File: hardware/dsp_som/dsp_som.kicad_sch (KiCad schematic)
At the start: 0 parts

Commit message: Tests
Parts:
- added C1: 2u2, Capacitor_SMD:C_0603_1608Metric, symbol Device:C_Small
- added FB1: 600R, Inductor_SMD:L_0603_1608Metric, symbol Device:FerriteBead_Small
- added H1: MountingHole_Pad, MountingHole:MountingHole_3.2mm_M3_Pad_Via, symbol Mechanical:MountingHole_Pad
- added J1: Micro_SD_Card_Det_Hirose_DM3AT, Connector_Card:microSD_HC_Hirose_DM3AT-SF-PEJM5, symbol Connector:Micro_SD_Card_Det_Hirose_DM3AT
- added J2: Conn_02x07_Odd_Even, Connector_PinHeader_1.27mm:PinHeader_2x07_P1.27mm_Vertical_SMD, symbol Connector_Generic:Conn_02x07_Odd_Even
- added J3: Conn_02x22_Odd_Even, Connector_PinHeader_2.54mm:PinHeader_2x22_P2.54mm_Vertical, symbol Connector_Generic:Conn_02x22_Odd_Even
- added U1: IS42S16400J-xT, Package_SO:TSOP-II-54_22.2x10.16mm_P0.8mm, symbol Memory_RAM:IS42S16400J-xT
- added U2: SGTL5000XNAA3, Package_DFN_QFN:QFN-32-1EP_5x5mm_P0.5mm_EP3.6x3.6mm, symbol Audio:SGTL5000XNAA3
- added U4: BU18SD2MG-MTR, Package_TO_SOT_SMD:SOT-23-5, symbol WITNS_ROHM:BU18SD2MG-MTR
- added U5: STM32F446ZCTx, Package_QFP:LQFP-144_20x20mm_P0.5mm, symbol MCU_ST_STM32F4:STM32F446ZCTx
- added Y1: 16MHz, Crystal:Crystal_SMD_EuroQuartz_MT-4Pin_3.2x2.5mm, symbol Device:Crystal_GND24_Small
- added Y3: 32kHz768, Crystal:Crystal_SMD_3215-2Pin_3.2x1.5mm, symbol Device:Crystal_Small
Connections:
- new net: U1.1 (VDD), U1.14 (VDD), U1.27 (VDD)
- new net: U1.12 (GNDQ), U1.46 (GNDQ), U1.52 (GNDQ), U1.6 (GNDQ)
- new net: U1.28 (GND), U1.41 (GND), U1.54 (GND)
- new net: U1.3 (VDDQ), U1.43 (VDDQ), U1.49 (VDDQ), U1.9 (VDDQ)
- new net: U5.107 (VSS), U5.120 (VSS), U5.130 (VSS), U5.16 (VSS), U5.38 (VSS), U5.51 (VSS), U5.61 (VSS), U5.83 (VSS), U5.94 (VSS)
- new net: U2.1 (GND), U2.3 (GND), U2.33 (GND)
- new net +3.3V: FB1.1
- new net +3.3VA: C1.1, FB1.2
- new net GND: C1.2, H1.1
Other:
- note added: "Farnell : 2101347"

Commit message: 1st attempt at routing the SDRAM
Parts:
- added C10, C11, C12, C13, C14, C15, C2, C22, C23, C24, C25, C26, C27, C28, C29, C3, C31, C4, C5, C6, C7, C8, C9: 100n, Capacitor_SMD:C_0402_1005Metric, symbol Device:C_Small
- added C16, C30, C32, C33, C34: 1u, Capacitor_SMD:C_0603_1608Metric, symbol Device:C_Small
- added C17: 4.7u, Capacitor_SMD:C_0603_1608Metric, symbol Device:C_Small
- added C18, C19: 10p, Capacitor_SMD:C_0402_1005Metric, symbol Device:C_Small
- added C20, C21: ??, Capacitor_SMD:C_0402_1005Metric, symbol Device:C_Small
- added R1: 10R, Resistor_SMD:R_0402_1005Metric, symbol Device:R_Small
- added R2: 100k, Resistor_SMD:R_0402_1005Metric, symbol Device:R_Small
- J2: value Conn_02x07_Odd_Even -> SWD
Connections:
- net +3.3V: now also J2.3 (Pin_3), U1.1 (VDD), U1.14 (VDD), U1.27 (VDD), U1.3 (VDDQ), U1.43 (VDDQ), U1.49 (VDDQ), U1.9 (VDDQ), U4.1 (IN), U4.3 (STBY), U5.108 (VDD), U5.121 (VDD), U5.131 (VDD), U5.143 (PDR_ON), U5.144 (VDD), U5.17 (VDD), U5.30 (VDD), U5.32 (VREF+), U5.39 (VDD), U5.52 (VDD), U5.6 (VBAT), U5.62 (VDD), U5.72 (VDD), U5.84 (VDD), U5.95 (VDDUSB), C10.1, C11.1, C12.1, C13.1, C14.1, C17.1, C22.1, C23.1, C24.1, C25.1, C26.1, C27.1, C28.1, C29.1, C3.1, C30.1, C31.1, C32.1, C33.1, C4.1, C5.1, C6.1, C7.1, C8.1, C9.1
- net +3.3VA: now also U5.33 (VDDA), C15.1, C16.1
- net GND: now also J2.11 (Pin_11), J2.5 (Pin_5), J2.7 (Pin_7), U1.12 (GNDQ), U1.28 (GND), U1.41 (GND), U1.46 (GNDQ), U1.52 (GNDQ), U1.54 (GND), U1.6 (GNDQ), U2.1 (GND), U2.3 (GND), U2.33 (GND), U2.7 (AGND), U4.2 (GND), U5.107 (VSS), U5.120 (VSS), U5.130 (VSS), U5.16 (VSS), U5.31 (VSSA), U5.38 (VSS), U5.51 (VSS), U5.61 (VSS), U5.83 (VSS), U5.94 (VSS), Y1.2, Y1.4, C10.2, C11.2, C12.2, C13.2, C14.2, C15.2, C16.2, C17.2, C18.1, C19.1, C2.2, C20.2, C21.2, C22.2, C23.2, C24.2, C25.2, C26.2, C27.2, C28.2, C29.2, C3.2, C30.2, C31.2, C32.2, C33.2, C34.2, C4.2, C5.2, C6.2, C7.2, C8.2, C9.2, R2.1
- net DQ5: now reaches U1.10 (DQ5)
- net DQ5: now also U5.59 (PE8)
- net DQ6: now reaches U1.11 (DQ6)
- net DQ6: now also U5.60 (PE9)
- net DQ7: now reaches U1.13 (DQ7)
- net DQ7: now also U5.63 (PE10)
- net LDQM: now reaches U1.15 (LDQM)
- net LDQM: now also U5.141 (PE0)
- net nWE: now reaches U1.16 (~{WE})
- net nWE: now also U5.26 (PC0)
- net nCAS: now reaches U1.17 (~{CAS})
- net nCAS: now also U5.132 (PG15)
- net nRAS: now reaches U1.18 (~{RAS})
- net nRAS: now also U5.49 (PF11)
- net nCS: now reaches U1.19 (~{CS})
- net nCS: now also U5.136 (PB6)
- net DQ0: now reaches U1.2 (DQ0)
- net DQ0: now also U5.85 (PD14)
- net BA0: now reaches U1.20 (BA0)
- net BA0: now also U5.89 (PG4)
- net BA1: now reaches U1.21 (BA1)
- net BA1: now also U5.90 (PG5)
- net A10: now reaches U1.22 (A10)
- net A10: now also U5.56 (PG0)
- net A0: now reaches U1.23 (A0)
- net A0: now also U5.10 (PF0)
- net A1: now reaches U1.24 (A1)
- net A1: now also U5.11 (PF1)
- net A2: now reaches U1.25 (A2)
- net A2: now also U5.12 (PF2)
- net A3: now reaches U1.26 (A3)
- net A3: now also U5.13 (PF3)
- net A4: now reaches U1.29 (A4)
- net A4: now also U5.14 (PF4)
- net A5: now reaches U1.30 (A5)
- net A5: now also U5.15 (PF5)
- net A6: now reaches U1.31 (A6)
- net A6: now also U5.50 (PF12)
- net A7: now reaches U1.32 (A7)
- net A7: now also U5.53 (PF13)
- net A8: now reaches U1.33 (A8)
- net A8: now also U5.54 (PF14)
- net A9: now reaches U1.34 (A9)
- net A9: now also U5.55 (PF15)
- net A11: now reaches U1.35 (A11)
- net A11: now also U5.57 (PG1)
- net CKE: now reaches U1.37 (CKE)
- net CKE: now also U5.135 (PB5)
- net CLK: now reaches U1.38 (CLK)
- net CLK: now also U5.93 (PG8)
- net UDQM: now reaches U1.39 (UDQM)
- net UDQM: now also U5.142 (PE1)
- net DQ1: now reaches U1.4 (DQ1)
- net DQ1: now also U5.86 (PD15)
- net DQ8: now reaches U1.42 (DQ8)
- net DQ8: now also U5.64 (PE11)
- net DQ9: now reaches U1.44 (DQ9)
- net DQ9: now also U5.65 (PE12)
- net DQ10: now reaches U1.45 (DQ10)
- net DQ10: now also U5.66 (PE13)
- net DQ11: now reaches U1.47 (DQ11)
- net DQ11: now also U5.67 (PE14)
- net DQ12: now reaches U1.48 (DQ12)
- net DQ12: now also U5.68 (PE15)
- net DQ2: now reaches U1.5 (DQ2)
- net DQ2: now also U5.114 (PD0)
- net DQ13: now reaches U1.50 (DQ13)
- net DQ13: now also U5.77 (PD8)
- net DQ14: now reaches U1.51 (DQ14)
- net DQ14: now also U5.78 (PD9)
- net DQ15: now reaches U1.53 (DQ15)
- net DQ15: now also U5.79 (PD10)
- net DQ3: now reaches U1.7 (DQ3)
- net DQ3: now also U5.115 (PD1)
- net DQ4: now reaches U1.8 (DQ4)
- net DQ4: now also U5.58 (PE7)
- net nRST: now reaches J2.12 (Pin_12)
- net nRST: now also U5.25 (NRST), C2.1
- net VCP_RX: now reaches J2.13 (Pin_13)
- net VCP_TX: now reaches J2.14 (Pin_14)
- net SWDIO: now reaches J2.4 (Pin_4)
- net SWDIO: now also U5.105 (PA13)
- net SWCLK: now reaches J2.6 (Pin_6)
- net SWCLK: now also U5.109 (PA14)
- net SWO: now reaches J2.8 (Pin_8)
- net SWO: now also U5.133 (PB3)
- net XTAL_OUT: now reaches Y1.1
- net XTAL_OUT: now also C19.2, R1.1
- net OSC_IN: now reaches Y1.3
- net OSC_IN: now also U5.23 (PH0), C18.2
- net BOOT0: now reaches U5.138 (BOOT0)
- net BOOT0: now also R2.2
- net OSC_OUT: now reaches U5.24 (PH1)
- net OSC_OUT: now also R1.2
- net OSC32_IN: now reaches U5.8 (PC14)
- net OSC32_IN: now also Y3.2, C20.1
- net OSC32_OUT: now reaches U5.9 (PC15)
- net OSC32_OUT: now also Y3.1, C21.1
- net +1V8: now reaches U4.5 (OUT)
- net +1V8: now also C34.1
- no-connect marks 0 -> 4
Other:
- note added: "Boot from Flash"
- note added: "Can't move"
- note added: "NBL0"
- note added: "NBL1"
- note added: "PA7/PC0"
- note added: "SDCKE1"
- note added: "SDCLK"
- note added: "SDNCAS"
- note added: "SDNE1"
- note added: "SDNRAS"
- note added: "SDNWE"
- moved on the sheet: J2, U1, U5, Y1, Y3

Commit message: routing 1st version
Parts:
- added C35, C36, C37, C38: 100n, Capacitor_SMD:C_0402_1005Metric, symbol Device:C_Small
- added C39, C40: 2.2u, Capacitor_SMD:C_0603_1608Metric, symbol Device:C_Small
- added R3, R4, R5, R6, R7: 47k, Resistor_SMD:R_0402_1005Metric, symbol Device:R_Small
- added R8, R9: 1.5k, Resistor_SMD:R_0402_1005Metric, symbol Device:R_Small
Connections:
- net +1V8: now also U2.30 (VDDD), C38.1
- net +3.3V: now also J1.4 (VDD), J3.1 (Pin_1), U2.20 (VDDIO), C35.1, R3.1, R4.1, R5.1, R6.1, R7.1, R8.1, R9.1
- net +3.3VA: now also U2.5 (VDDA), C37.1
- net GND: now also J1.11 (SHIELD), J1.6 (VSS), J1.9 (DET_B), J3.10 (Pin_10), J3.12 (Pin_12), J3.14 (Pin_14), J3.16 (Pin_16), J3.18 (Pin_18), J3.2 (Pin_2), J3.20 (Pin_20), J3.22 (Pin_22), J3.24 (Pin_24), J3.26 (Pin_26), J3.28 (Pin_28), J3.30 (Pin_30), J3.32 (Pin_32), J3.34 (Pin_34), J3.35 (Pin_35), J3.36 (Pin_36), J3.38 (Pin_38), J3.4 (Pin_4), J3.40 (Pin_40), J3.42 (Pin_42), J3.44 (Pin_44), J3.6 (Pin_6), J3.8 (Pin_8), U2.31 (CTRL_ADR0_CS), U2.32 (CTRL_MODE), C35.2, C36.2, C37.2, C38.2, C39.2, C40.2
- net VCP_RX: now also U5.35 (PA1)
- net VCP_TX: now also U5.34 (PA0)
- net SD_DAT2: now reaches J1.1 (DAT2)
- net SD_DAT2: now also U5.111 (PC10), R7.2
- net SD_DETECT: now reaches J1.10 (DET_A)
- net SD_DETECT: now also U5.137 (PB7)
- net SD_DAT3: now reaches J1.2 (DAT3/CD)
- net SD_DAT3: now also U5.112 (PC11), R6.2
- net SD_CMD: now reaches J1.3 (CMD)
- net SD_CMD: now also U5.116 (PD2), R5.2
- net SD_CLK: now reaches J1.5 (CLK)
- net SD_CLK: now also U5.113 (PC12)
- net SD_DAT0: now reaches J1.7 (DAT0)
- net SD_DAT0: now also U5.98 (PC8), R4.2
- net SD_DAT1: now reaches J1.8 (DAT1)
- net SD_DAT1: now also U5.99 (PC9), R3.2
- net CODEC_MCLK: now reaches U5.1 (PE2)
- net CODEC_MCLK: now also U2.21 (SYS_MCLK)
- net USB_DM: now reaches U5.103 (PA11)
- net USB_DM: now also J3.25 (Pin_25)
- net USB_DP: now reaches U5.104 (PA12)
- net USB_DP: now also J3.27 (Pin_27)
- net VCAP_2: now reaches U5.106 (VCAP_2)
- net VCAP_2: now also C39.1
- net CODEC_SCL: now reaches U5.139 (PB8)
- net CODEC_SCL: now also U2.29 (CTRL_CLK), R8.2
- net CODEC_SDA: now reaches U5.140 (PB9)
- net CODEC_SDA: now also U2.27 (CTRL_DATA), R9.2
- net ADC3_IN4: now reaches U5.18 (PF6)
- net ADC3_IN4: now also J3.33 (Pin_33)
- net ADC3_IN5: now reaches U5.19 (PF7)
- net ADC3_IN5: now also J3.31 (Pin_31)
- net CODEC_DOUT: now reaches U5.2 (PE3)
- net CODEC_DOUT: now also U2.25 (I2S_DOUT)
- net ADC3_IN6: now reaches U5.20 (PF8)
- net ADC3_IN6: now also J3.29 (Pin_29)
- net ADC3_IN7: now reaches U5.21 (PF9)
- net ADC3_IN7: now also J3.23 (Pin_23)
- net ADC3_IN8: now reaches U5.22 (PF10)
- net ADC3_IN8: now also J3.21 (Pin_21)
- net ADC3_IN11: now reaches U5.27 (PC1)
- net ADC3_IN11: now also J3.19 (Pin_19)
- net ADC3_IN12: now reaches U5.28 (PC2)
- net ADC3_IN12: now also J3.17 (Pin_17)
- net ADC3_IN13: now reaches U5.29 (PC3)
- net ADC3_IN13: now also J3.15 (Pin_15)
- net CODEC_LRCLK: now reaches U5.3 (PE4)
- net CODEC_LRCLK: now also U2.23 (I2S_LRCLK)
- net ADC3_IN2: now reaches U5.36 (PA2)
- net ADC3_IN2: now also J3.11 (Pin_11)
- net ADC3_IN3: now reaches U5.37 (PA3)
- net ADC3_IN3: now also J3.13 (Pin_13)
- net CODEC_SCLK: now reaches U5.4 (PE5)
- net CODEC_SCLK: now also U2.24 (I2S_SCLK)
- net CODEC_DIN: now reaches U5.5 (PE6)
- net CODEC_DIN: now also U2.26 (I2S_DIN)
- net PB10: now reaches U5.69 (PB10)
- net PB10: now also J3.3 (Pin_3)
- net PB11: now reaches U5.70 (PB11)
- net PB11: now also J3.5 (Pin_5)
- net VCAP_1: now reaches U5.71 (VCAP_1)
- net VCAP_1: now also C40.1
- net PD12: now reaches U5.81 (PD12)
- net PD12: now also J3.7 (Pin_7)
- net PD13: now reaches U5.82 (PD13)
- net PD13: now also J3.9 (Pin_9)
- net LINEOUT_R: now reaches J3.37 (Pin_37)
- net LINEOUT_R: now also U2.11 (LINEOUT_R)
- net LINEOUT_L: now reaches J3.39 (Pin_39)
- net LINEOUT_L: now also U2.12 (LINEOUT_L)
- net LINEIN_R: now reaches J3.41 (Pin_41)
- net LINEIN_R: now also U2.13 (LINEIN_R)
- net LINEIN_L: now reaches J3.43 (Pin_43)
- net LINEIN_L: now also U2.14 (LINEIN_L)
- net VAG: now reaches U2.10 (VAG)
- net VAG: now also C36.1
- no-connect marks 4 -> 47
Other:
- note added: "I2C Mode"
- note added: "VDDIO & VDDA to 3.3V => No CPFILT"
- note removed: "Can't move"
- moved on the sheet: C1, C33, C34, FB1, J3, U2, U4

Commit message: gnd vias
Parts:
- J3: value Conn_02x22_Odd_Even -> DSP_SoM Connector
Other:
- note added: "CODEC VDDD LDO"
- note added: "DSP SoM Connector"
- note added: "Micro SD-Card Socket"
- note added: "Mounting Hole"
- note added: "SDRAM"
- note added: "SGTL5000 Audio CODEC"
- note added: "SWD Connector for STLINK"
- note added: "The STM32"
- note added: "VDDA Filtering"
- company: (none) -> WITNS
- title: (none) -> DSP SoM
- moved on the sheet: C1, C10, C11, C12, C13, C14, C15, C16, C17, C18, C19, C2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

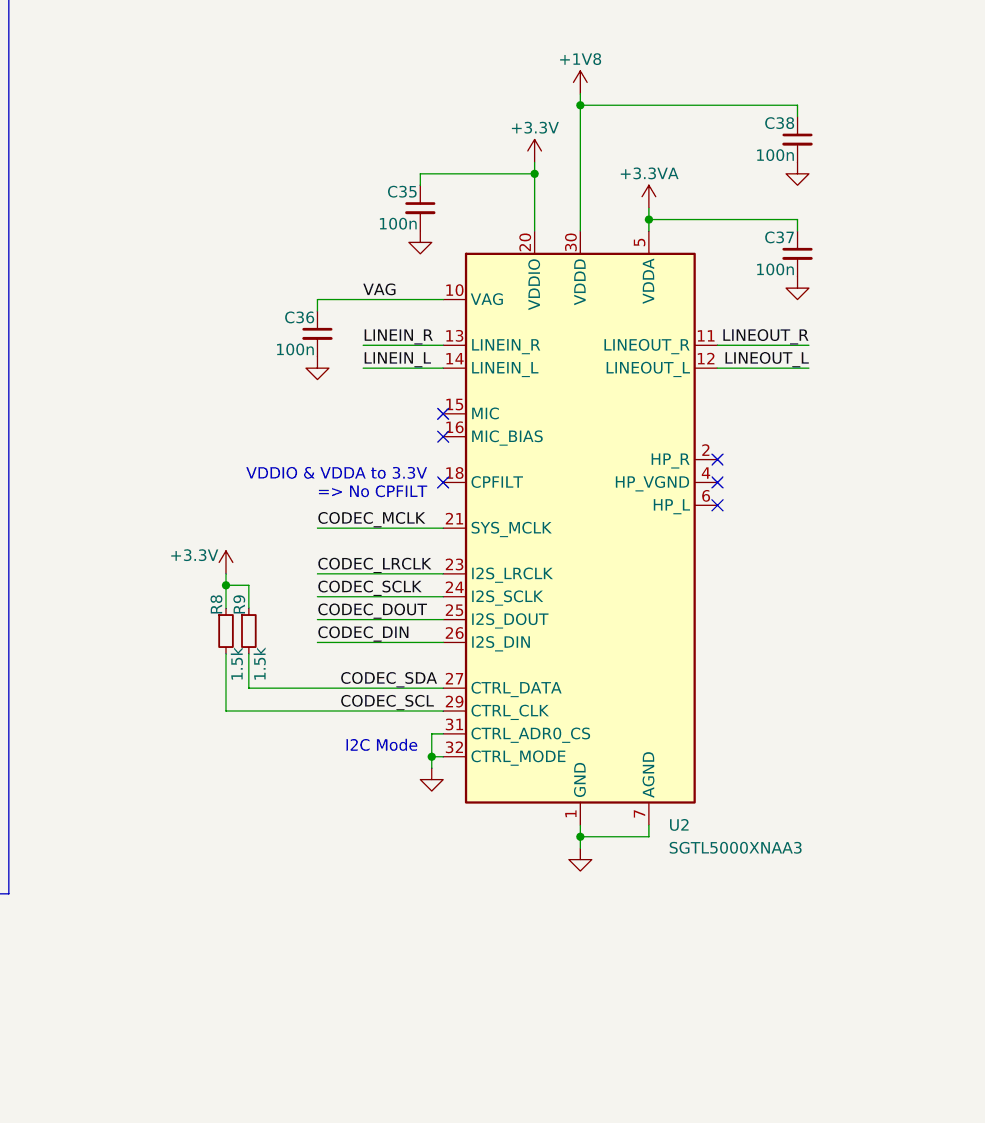
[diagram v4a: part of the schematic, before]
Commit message: Change SGTL5000 model due to obsolescence
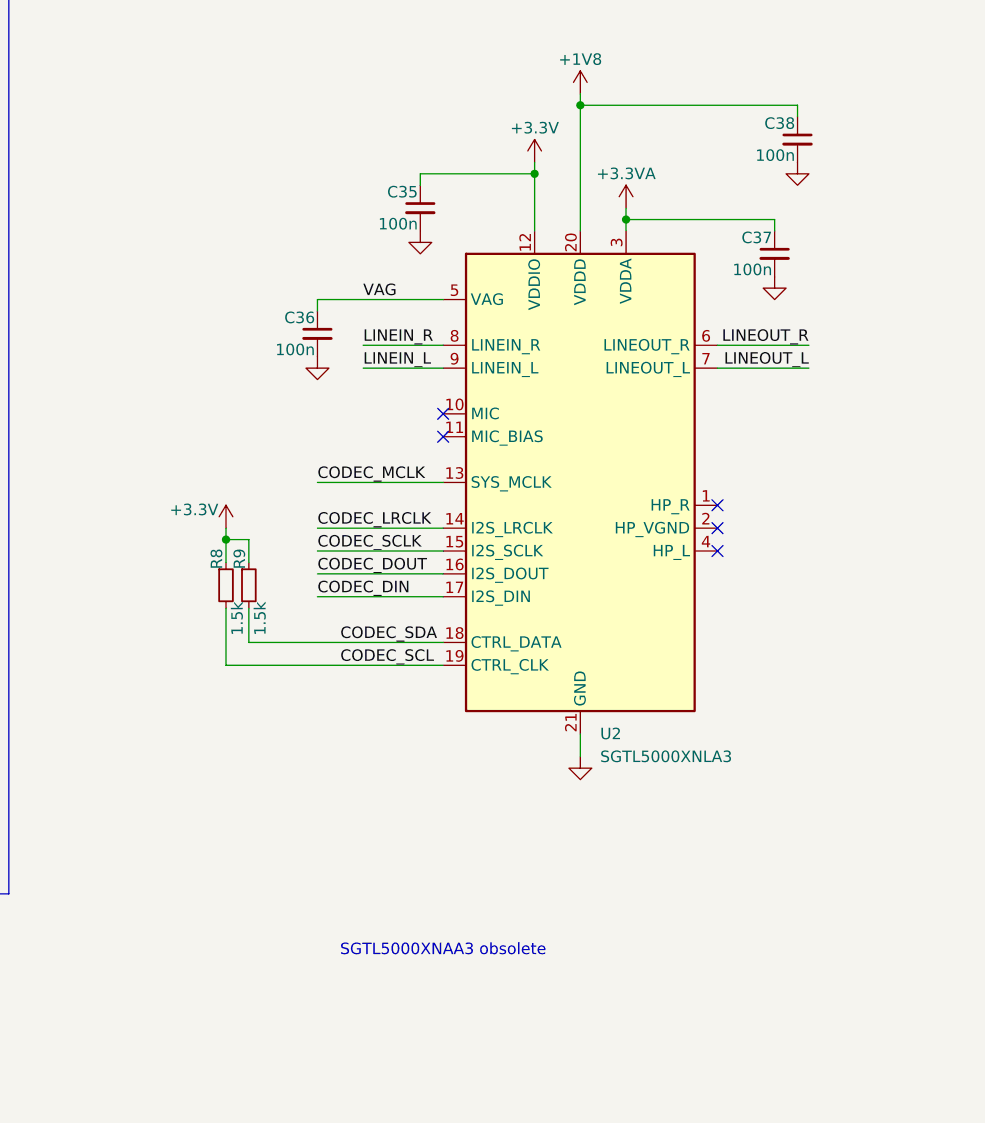
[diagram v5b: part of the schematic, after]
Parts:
- removed U2: SGTL5000XNAA3, Package_DFN_QFN:QFN-32-1EP_5x5mm_P0.5mm_EP3.6x3.6mm, symbol Audio:SGTL5000XNAA3
- added U2: SGTL5000XNLA3, Package_DFN_QFN:QFN-20-1EP_3x3mm_P0.4mm_EP1.65x1.65mm, symbol Audio:SGTL5000XNLA3
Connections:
- net +1V8: now also U2.20 (VDDD)
- net +3.3V: now also U2.12 (VDDIO)
- net +3.3VA: now also U2.3 (VDDA)
- net CODEC_DIN: now also U2.17 (I2S_DIN)
- net CODEC_DOUT: now also U2.16 (I2S_DOUT)
- net CODEC_LRCLK: now also U2.14 (I2S_LRCLK)
- net CODEC_MCLK: now also U2.13 (SYS_MCLK)
- net CODEC_SCL: now also U2.19 (CTRL_CLK)
- net CODEC_SCLK: now also U2.15 (I2S_SCLK)
- net CODEC_SDA: now also U2.18 (CTRL_DATA)
- net GND: now also U2.21 (GND)
- net LINEIN_L: now also U2.9 (LINEIN_L)
- net LINEIN_R: now also U2.8 (LINEIN_R)
- net LINEOUT_L: now also U2.7 (LINEOUT_L)
- net LINEOUT_R: now also U2.6 (LINEOUT_R)
- net VAG: now also U2.5 (VAG)
- no-connect marks 47 -> 46
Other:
- note added: "SGTL5000XNAA3 obsolete"
- note removed: "I2C Mode"
- note removed: "VDDIO & VDDA to 3.3V => No CPFILT"
- moved on the sheet: C37, R8, R9
